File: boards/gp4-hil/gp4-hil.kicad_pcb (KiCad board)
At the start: 4 copper layers, 160 x 60 mm, 488 parts, among them J1 BEL_FUSE_0826-1G1T-23-F, J2 XILINX_JTAG, J3 XILINX_JTAG_ICESIDE, J4 XILINX_JTAG_ICESIDE, K1 CONN_3_PWROUT, P1 GPAK_ZIF, P2 2x10 HEADER, Q1 SSM6N58NU, Q11 SSM6N58NU, Q12 DMP2069UFY4, Q13 SSM6N58NU, Q14 SSM6N58NU, Q15 SSM6N58NU, Q16 SSM6N58NU, Q17 SSM6N58NU, Q18 SSM6N58NU, Q19 SSM6N58NU, Q20 SSM6N58NU, Q21 SSM6N58NU, Q22 DMP2069UFY4, U1 MIC2288-DFN, U10 AD9609, U11 DAC084S085, U12 DAC084S085, U13 DAC084S085, U14 DAC084S085, U15 TS3A4751, U16 TS3A4751, U17 TS3A4751, U18 TS3A4751, U19 TS3A4751, U2 XC7A100T-1FTG256C, U20 SIP32408, U21 SIP32408, U22 SIP32408, U23 SIP32408, U24 SIP32408, U25 TS3A4751, U26 TS3A4751, U27 TS3A4751, U28 TS3A4751, U29 TXB0104RUT, U3 LTC3374-QFN, U30 TXB0104RUT, U31 ADA4937-2, U32 SIP32408, U33 125 MHz, U34 INA199A2RSW, U35 INA199A2RSW, U36 INA199A2RSW, U4 SIP32408, U5 KSZ9031RN, U6 W25Q32FW, U7 25 MHz, U8 ADG726, U9 AD9609

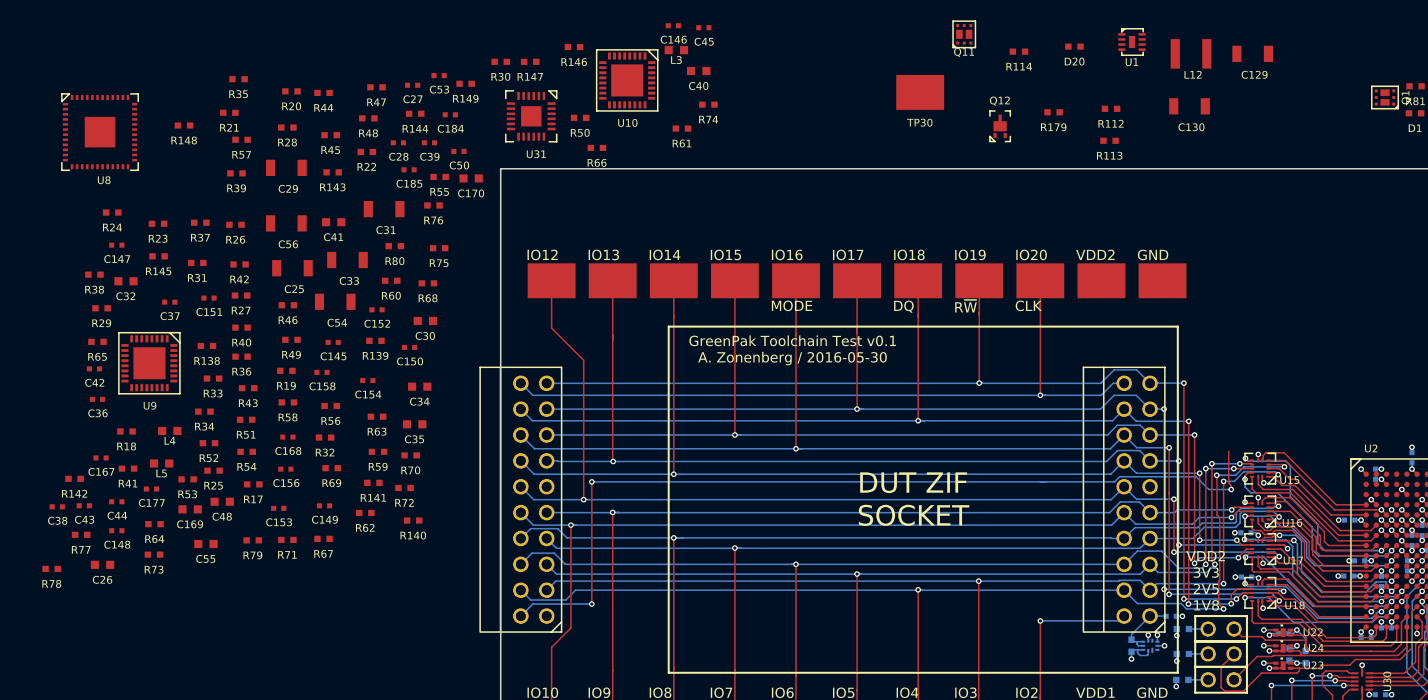
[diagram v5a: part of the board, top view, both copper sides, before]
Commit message: Began work on analog mux input routing. Needs more work.
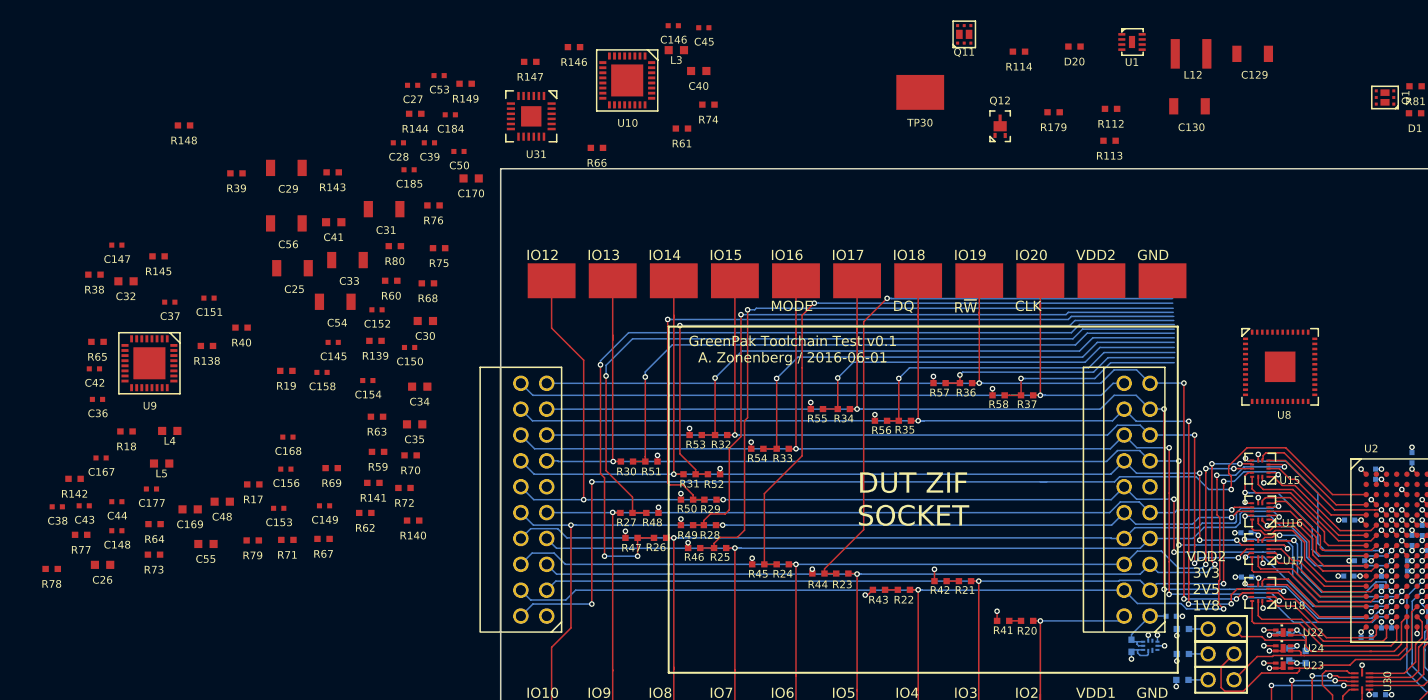
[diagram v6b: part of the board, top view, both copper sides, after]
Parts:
- moved U8 118.2 mm to (97.5, 79.5)
- moved R20 89.0 mm to (72.7, 104.4)
- moved R41 87.2 mm to (70.3, 104.4)
- moved R21 85.7 mm to (66.6, 100.5)
- moved R37 83.0 mm to (72.7, 82.2)
- moved R42 75.5 mm to (64.2, 100.5)
- moved R23 75.5 mm to (54.5, 99.8)
- moved R24 74.4 mm to (48.7, 98.8)
- moved R35 73.5 mm to (60.7, 84.8)
- moved R57 72.6 mm to (64.1, 81.0)
- moved R36 71.2 mm to (66.7, 81.0)
- moved R58 69.8 mm to (69.9, 82.2)
- moved R22 68.1 mm to (60.6, 101.3)
- moved R44 67.8 mm to (52.2, 99.8)
- moved R43 65.0 mm to (58.1, 101.3)
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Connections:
- R33 pad 1: /Analog IO/ADC_IN15 -> /Analog IO/ADC_IN16
- R34 pad 1: /Analog IO/ADC_IN16 -> /Analog IO/ADC_IN17
- R35 pad 1: /Analog IO/ADC_IN17 -> /Analog IO/ADC_IN18
- R36 pad 1: /Analog IO/ADC_IN18 -> /Analog IO/ADC_IN19
- R37 pad 1: /Analog IO/ADC_IN19 -> /Analog IO/ADC_IN20
- R54 pad 2: /Analog IO/ADC_IN15 -> /Analog IO/ADC_IN16
- R55 pad 2: /Analog IO/ADC_IN16 -> /Analog IO/ADC_IN17
- R56 pad 2: /Analog IO/ADC_IN17 -> /Analog IO/ADC_IN18
- R57 pad 2: /Analog IO/ADC_IN18 -> /Analog IO/ADC_IN19
- R58 pad 2: /Analog IO/ADC_IN19 -> /Analog IO/ADC_IN20
- U2 pad B1: /DUT/GPIO2_DIO -> (no net)
- U2 pad C1: (no net) -> /DUT/GPIO2_DIO
- U8 pad 35: /Analog IO/PSU_VTEMP -> /Analog IO/ADC_IN20
- U8 pad 36: /Analog IO/VDD2_ISENSE -> /Analog IO/PSU_VTEMP
- U8 pad 37: (no net) -> /Analog IO/VDD2_ISENSE
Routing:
- net /Analog IO/GND: track 866.0 -> 981.9 mm, vias 146 -> 164
- net /Analog IO/ADC_IN9: track 0.00 -> 83.8 mm, vias 0 -> 3
- net /Analog IO/ADC_IN10: track 0.00 -> 74.2 mm, vias 0 -> 1
- net /Analog IO/ADC_IN12: track 0.00 -> 70.4 mm, vias 0 -> 1
- net /Analog IO/ADC_IN8: track 0.00 -> 69.0 mm, vias 0 -> 1
- net /Analog IO/ADC_IN11: track 0.00 -> 66.6 mm, vias 0 -> 1
- net /Analog IO/ADC_IN14: track 0.00 -> 65.2 mm, vias 0 -> 1
- net /Analog IO/ADC_IN7: track 0.00 -> 64.1 mm, vias 0 -> 1
- net /Analog IO/ADC_IN13: track 0.00 -> 63.5 mm, vias 0 -> 1
- net /Analog IO/ADC_IN6: track 0.00 -> 58.8 mm, vias 0 -> 1
- net /Analog IO/ADC_IN15: track 0.00 -> 53.6 mm, vias 0 -> 1
- net /Analog IO/ADC_IN16: track 0.00 -> 48.7 mm, vias 0 -> 1
- net /Analog IO/ADC_IN17: track 0.00 -> 38.8 mm, vias 0 -> 1
- net /Analog IO/ADC_IN18: track 0.00 -> 33.5 mm, vias 0 -> 1
- net /Analog IO/ADC_IN19: track 0.00 -> 24.0 mm, vias 0 -> 1
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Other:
- board text added: "GreenPak Toolchain Test v0.1 A. Zonenberg / 2016-06-01"
- board text removed: "GreenPak Toolchain Test v0.1 A. Zonenberg / 2016-05-30"

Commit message: Saving current layout before tweaking attenuators
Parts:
- moved R142 132.9 mm to (109.2, 63.0), turned to 90 degrees
- moved R145 118.1 mm to (105.5, 70.7)
- moved R148 116.4 mm to (105.7, 67.8), turned to 180 degrees
- moved C26 111.7 mm to (90.6, 73.0), turned to 270 degrees
- moved R143 101.4 mm to (105.7, 66.0), turned to 180 degrees
- moved C29 94.9 mm to (93.6, 75.2), turned to 270 degrees
- moved R144 94.2 mm to (105.7, 68.7), turned to 180 degrees
- moved C25 89.8 mm to (90.2, 75.5)
- moved U31 87.5 mm to (110.6, 67.3), turned to 90 degrees
- moved R147 83.6 mm to (105.7, 66.9), turned to 180 degrees
- moved R146 83.3 mm to (110.1, 63.0), turned to 90 degrees
- moved Q13 79.9 mm to (53.5, 133.6)
- moved L3 59.6 mm to (92.8, 72.3), turned to 180 degrees
- moved Q14 47.7 mm to (40.4, 134.7)
- moved C178 47.2 mm to (79.9, 141.8)
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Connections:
- U8 pad 1: (no net) -> /Analog IO/ADC_IN8
- U8 pad 10: /Analog IO/ADC_IN6 -> /Analog IO/ADC_IN17
- U8 pad 11: /Analog IO/ADC_IN5 -> /Analog IO/ADC_IN18
- U8 pad 12: /Analog IO/ADC_IN4 -> /Analog IO/ADC_IN19
- U8 pad 2: (no net) -> /Analog IO/ADC_IN11
- U8 pad 25: /Analog IO/ADC_IN11 -> /Analog IO/VDD2_ISENSE
- U8 pad 26: /Analog IO/ADC_IN12 -> /Analog IO/ADC_IN20
- U8 pad 27: /Analog IO/ADC_IN13 -> /Analog IO/VPP_ISENSE
- U8 pad 28: /Analog IO/ADC_IN14 -> /Analog IO/VDD1_ISENSE
- U8 pad 29: /Analog IO/ADC_IN15 -> /Analog IO/ADC_IN3
- U8 pad 3: (no net) -> /Analog IO/ADC_IN12
- U8 pad 30: /Analog IO/ADC_IN15 -> /Analog IO/ADC_IN1
- U8 pad 31: /Analog IO/ADC_IN16 -> /Analog IO/ADC_IN2
- U8 pad 32: /Analog IO/ADC_IN17 -> /Analog IO/ADC_IN0
- U8 pad 33: /Analog IO/ADC_IN18 -> /Analog IO/PSU_VTEMP
- U8 pad 34: /Analog IO/ADC_IN19 -> (no net)
- U8 pad 35: /Analog IO/ADC_IN20 -> (no net)
- U8 pad 36: /Analog IO/PSU_VTEMP -> (no net)
- U8 pad 37: /Analog IO/VDD2_ISENSE -> (no net)
- U8 pad 4: /Analog IO/VDD1_ISENSE -> /Analog IO/ADC_IN14
- U8 pad 45: /Analog IO/ADC_IN3 -> /Analog IO/ADC_IN4
- U8 pad 46: /Analog IO/ADC_IN2 -> /Analog IO/ADC_IN5
- U8 pad 47: /Analog IO/ADC_IN1 -> /Analog IO/ADC_IN6
- U8 pad 48: /Analog IO/ADC_IN0 -> /Analog IO/ADC_IN7
- U8 pad 5: /Analog IO/VPP_ISENSE -> /Analog IO/ADC_IN9
- U8 pad 7: /Analog IO/ADC_IN9 -> /Analog IO/ADC_IN13
- U8 pad 8: /Analog IO/ADC_IN8 -> /Analog IO/ADC_IN15
- U8 pad 9: /Analog IO/ADC_IN7 -> /Analog IO/ADC_IN16
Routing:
- net /Analog IO/GND: track 981.9 -> 1075.3 mm, vias 164 -> 188
- net /Analog IO/ADC_IN5: track 1.26 -> 68.3 mm, vias 0 -> 2
- net /Analog IO/ADC_IN4: track 1.21 -> 62.9 mm, vias 0 -> 2
- net /Analog IO/PSU_VTEMP: track 12.1 -> 57.7 mm, vias 0 -> 2
- net /Analog IO/ADC_IN3: track 1.16 -> 36.7 mm, vias 0 -> 1
- net /Analog IO/2V5: track 186.9 -> 202.8 mm, vias 18 -> 25
- net /Analog IO/ADC_A_VIN: track 0.00 -> 15.1 mm
- net /Analog IO/ADC_B_VIN: track 0.00 -> 14.6 mm
- net /Analog IO/ADC_IN6: track 58.8 -> 71.0 mm, vias 1 -> 2
- net /Analog IO/A2V5: track 0.00 -> 12.2 mm, vias 0 -> 5
- net /Analog IO/ADC_IN7: track 64.1 -> 74.7 mm, vias 1 -> 2
- net /Analog IO/ADC_IN8: track 69.0 -> 79.0 mm, vias 1 -> 2
- net /Analog IO/ADC_IN11: track 66.6 -> 76.4 mm, vias 1 -> 2
- net /Analog IO/ADC_IN12: track 70.4 -> 80.2 mm, vias 1 -> 2
- net /Analog IO/ADC_IN14: track 65.2 -> 74.8 mm, vias 1 -> 2
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
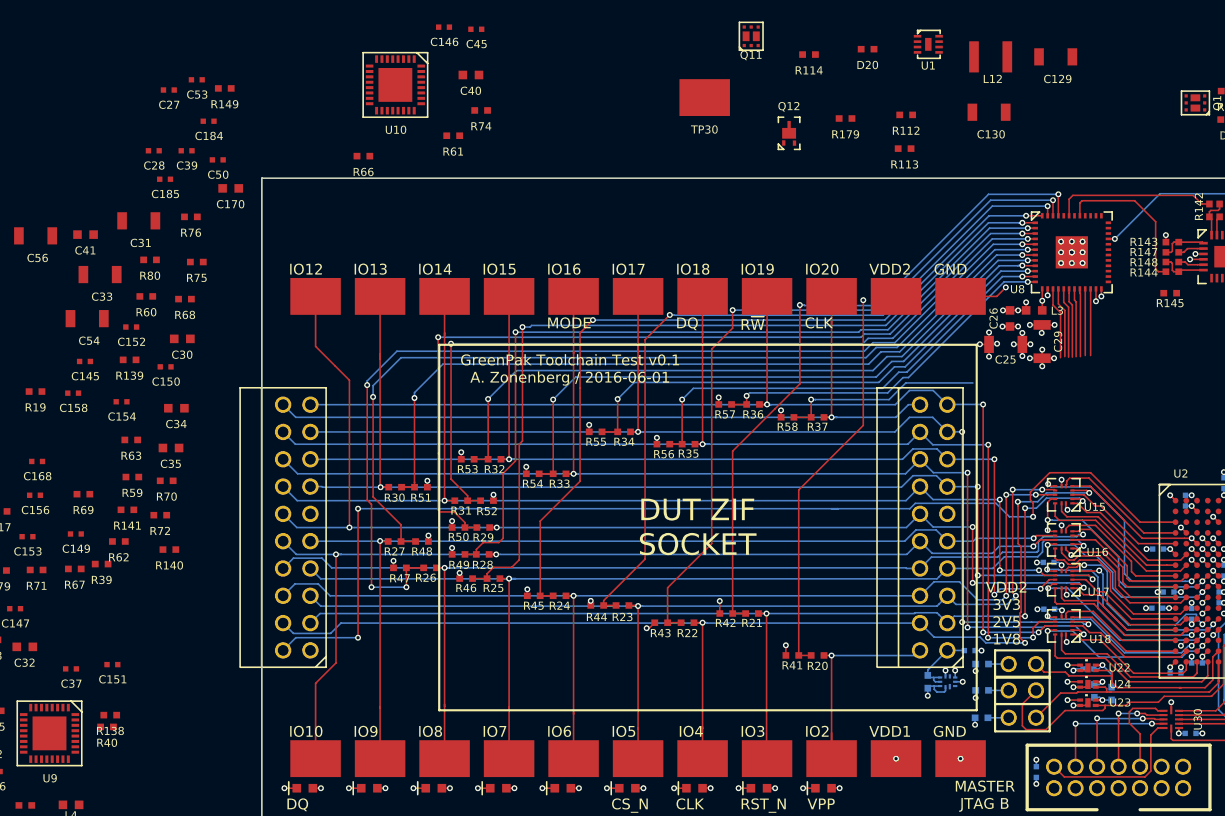
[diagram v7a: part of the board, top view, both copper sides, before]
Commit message: Massive cleanup of analog input logic. Deleted a couple dozen components, got higher input bandwidth, reduced BOM cost. What's not to like?
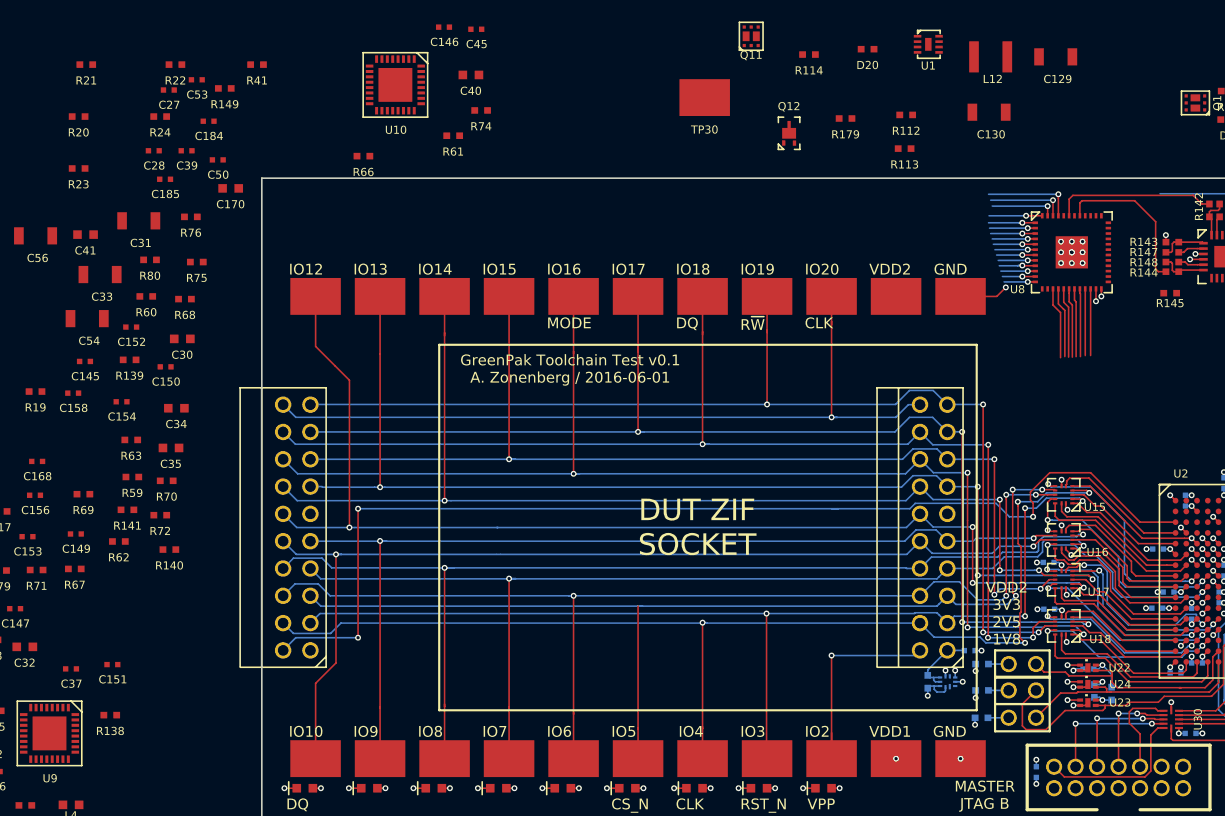
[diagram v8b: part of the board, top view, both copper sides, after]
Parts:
- removed C25, C29: 47 uF, azonenberg_pcb:EIA_1206_CAP_NOSILK
- removed C26: 4.7 uF, azonenberg_pcb:EIA_0603_CAP_NOSILK
- removed L3: 600R, azonenberg_pcb:EIA_0603_INDUCTOR_NOSILK
- removed R25, R26, R27, R28, R29, R30, R31, R32, R33, R34, R35, R36, R37: 30K 0.1%, azonenberg_pcb:EIA_0402_RES_NOSILK
- removed R39, R40, R42, R43, R44, R45, R46, R47, R48, R49, R50, R51, R52, R53, R54, R55, R56, R57, R58: 10K 0.1%, azonenberg_pcb:EIA_0402_RES_NOSILK
- R142, R143: value 100K 0.1% -> 40.2K 0.1%
- R146, R147: value 100K 0.1% -> 10K 0.1%
- R22, R23, R24: value 30K 0.1% -> 10K 0.1%
- moved R20 85.1 mm to (3.95, 54.3)
- moved R21 80.3 mm to (4.67, 49.4)
- moved R41 74.2 mm to (20.6, 49.4)
- moved R22 70.5 mm to (13.0, 49.4)
- moved R23 64.9 mm to (3.95, 59.1)
- moved R24 58.0 mm to (11.5, 54.3)
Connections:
- C27 pad 1: /Analog IO/A2V5 -> /Analog IO/A3V3
- C28 pad 1: /Analog IO/A2V5 -> /Analog IO/A3V3
- C30 pad 1: /Analog IO/A2V5 -> /Analog IO/A3V3
- R17 pad 1: /Analog IO/ADC_IN1 -> /Analog IO/ADC_GPIO20
- R17 pad 2: /Analog IO/DUT_VDD1 -> /Analog IO/DUT_GPIO20
- R18 pad 1: /Analog IO/ADC_IN0 -> /Analog IO/ADC_VPP
- R19 pad 1: /Analog IO/ADC_IN2 -> /Analog IO/ADC_VDD1
- R19 pad 2: /Analog IO/DUT_VDD2 -> /Analog IO/DUT_VDD1
- R20 pad 1: /Analog IO/ADC_IN3 -> /Analog IO/ADC_GPIO2
- R21 pad 1: /Analog IO/ADC_IN4 -> /Analog IO/ADC_VDD2
- R21 pad 2: /Analog IO/DUT_GPIO3 -> /Analog IO/DUT_VDD2
- R22 pad 1: /Analog IO/ADC_IN5 -> /Analog IO/GND
- R22 pad 2: /Analog IO/DUT_GPIO4 -> /Analog IO/ADC_GPIO20
- R23 pad 1: /Analog IO/ADC_IN6 -> /Analog IO/GND
- R23 pad 2: /Analog IO/DUT_GPIO5 -> /Analog IO/ADC_VDD1
- R24 pad 1: /Analog IO/ADC_IN7 -> /Analog IO/GND
- R24 pad 2: /Analog IO/DUT_GPIO6 -> /Analog IO/ADC_VDD2
- R38 pad 2: /Analog IO/ADC_IN0 -> /Analog IO/ADC_VPP
- R41 pad 2: /Analog IO/ADC_IN3 -> /Analog IO/ADC_GPIO2
- U8 pad 1: /Analog IO/ADC_IN8 -> /Analog IO/DUT_GPIO19
- U8 pad 10: /Analog IO/ADC_IN17 -> /Analog IO/DUT_GPIO9
- U8 pad 11: /Analog IO/ADC_IN18 -> /Analog IO/DUT_GPIO8
- U8 pad 12: /Analog IO/ADC_IN19 -> /Analog IO/DUT_GPIO7
- U8 pad 13: /Analog IO/A2V5 -> /Analog IO/A3V3
- U8 pad 14: /Analog IO/A2V5 -> /Analog IO/A3V3
- U8 pad 2: /Analog IO/ADC_IN11 -> /Analog IO/DUT_GPIO18
- U8 pad 25: /Analog IO/VDD2_ISENSE -> /Analog IO/ADC_VPP
- U8 pad 26: /Analog IO/ADC_IN20 -> /Analog IO/VPP_ISENSE
- U8 pad 27: /Analog IO/VPP_ISENSE -> /Analog IO/VDD1_ISENSE
- U8 pad 28: /Analog IO/VDD1_ISENSE -> /Analog IO/VDD2_ISENSE
- U8 pad 29: /Analog IO/ADC_IN3 -> /Analog IO/PSU_VTEMP
- U8 pad 3: /Analog IO/ADC_IN12 -> /Analog IO/DUT_GPIO17
- U8 pad 30: /Analog IO/ADC_IN1 -> /Analog IO/ADC_GPIO2
- U8 pad 31: /Analog IO/ADC_IN2 -> /Analog IO/ADC_GPIO20
- U8 pad 32: /Analog IO/ADC_IN0 -> /Analog IO/ADC_VDD1
- U8 pad 33: /Analog IO/PSU_VTEMP -> /Analog IO/ADC_VDD2
- U8 pad 4: /Analog IO/ADC_IN14 -> /Analog IO/DUT_GPIO16
- U8 pad 45: /Analog IO/ADC_IN4 -> /Analog IO/DUT_GPIO6
- U8 pad 46: /Analog IO/ADC_IN5 -> /Analog IO/DUT_GPIO5
- U8 pad 47: /Analog IO/ADC_IN6 -> /Analog IO/DUT_GPIO4
- U8 pad 48: /Analog IO/ADC_IN7 -> /Analog IO/DUT_GPIO3
- U8 pad 5: /Analog IO/ADC_IN9 -> /Analog IO/DUT_GPIO15
- U8 pad 6: /Analog IO/ADC_IN10 -> /Analog IO/DUT_GPIO14
- U8 pad 7: /Analog IO/ADC_IN13 -> /Analog IO/DUT_GPIO13
- U8 pad 8: /Analog IO/ADC_IN15 -> /Analog IO/DUT_GPIO12
- U8 pad 9: /Analog IO/ADC_IN16 -> /Analog IO/DUT_GPIO10
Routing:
- net /Analog IO/GND: track 1075.3 -> 933.1 mm, vias 188 -> 160
- net /Analog IO/ADC_IN9: track 93.4 -> 0.00 mm, vias 4 -> 0
- net /Analog IO/ADC_IN10: track 83.8 -> 0.00 mm, vias 2 -> 0
- net /Analog IO/ADC_IN12: track 80.2 -> 0.00 mm, vias 2 -> 0
- net /Analog IO/ADC_IN8: track 79.0 -> 0.00 mm, vias 2 -> 0
- net /Analog IO/ADC_IN11: track 76.4 -> 0.00 mm, vias 2 -> 0
- net /Analog IO/ADC_IN14: track 74.8 -> 0.00 mm, vias 2 -> 0
- net /Analog IO/ADC_IN7: track 74.7 -> 0.00 mm, vias 2 -> 0
- net /Analog IO/ADC_IN13: track 73.1 -> 0.00 mm, vias 2 -> 0
- net /Analog IO/ADC_IN6: track 71.0 -> 0.00 mm, vias 2 -> 0
- net /Analog IO/ADC_IN5: track 68.3 -> 0.00 mm, vias 2 -> 0
- net /Analog IO/ADC_IN15: track 63.2 -> 0.00 mm, vias 2 -> 0
- net /Analog IO/ADC_IN4: track 62.9 -> 0.00 mm, vias 2 -> 0
- net /Analog IO/ADC_IN16: track 58.2 -> 0.00 mm, vias 2 -> 0
- net /Analog IO/ADC_IN17: track 48.3 -> 0.00 mm, vias 2 -> 0
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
